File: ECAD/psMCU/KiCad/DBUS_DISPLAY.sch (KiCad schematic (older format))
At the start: 9 parts, among them U50 SN74LVC1G04DCK, U51 SN74HC245PW

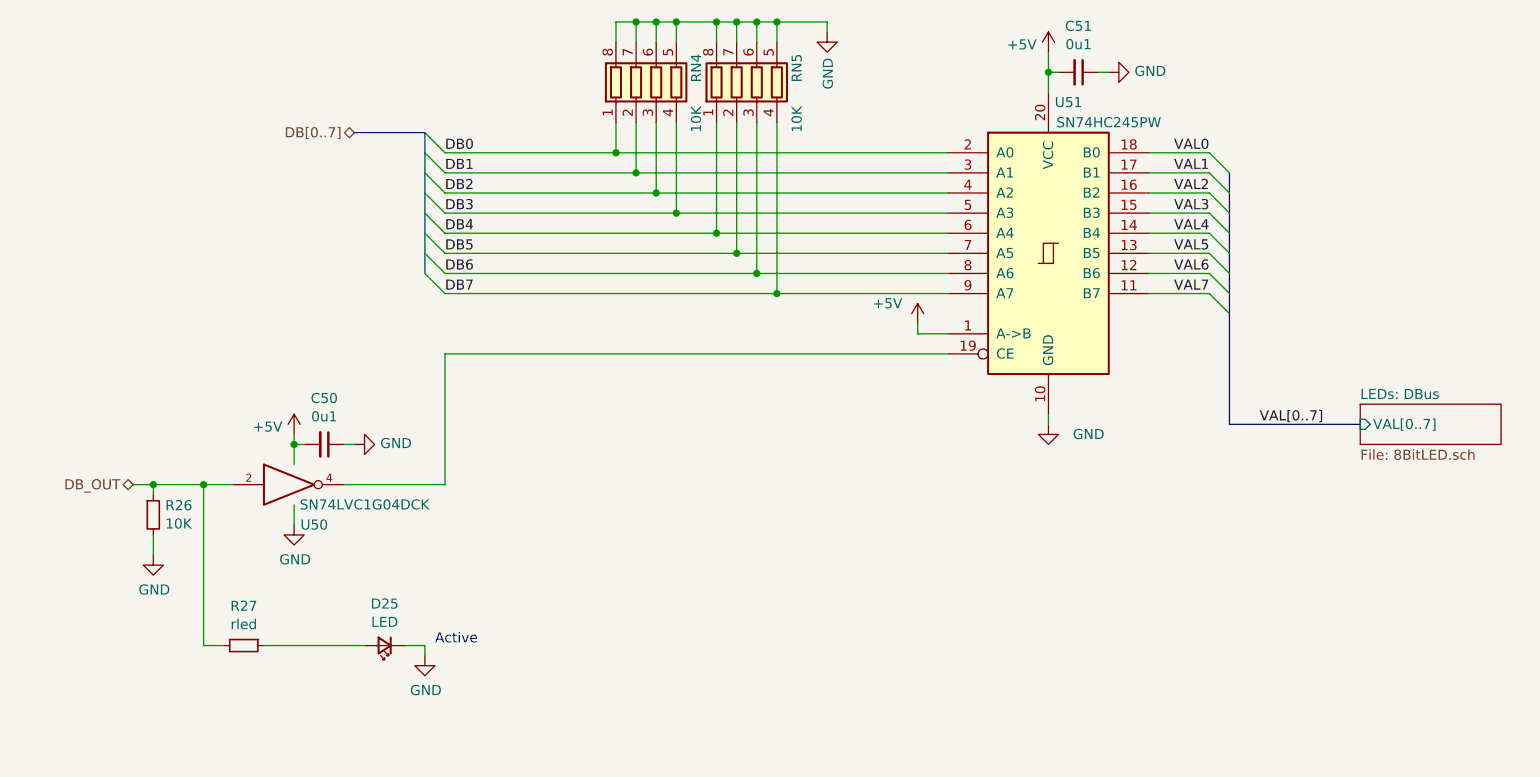
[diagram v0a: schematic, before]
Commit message: Sch: Reworked Peripheral Interface (Buffers)
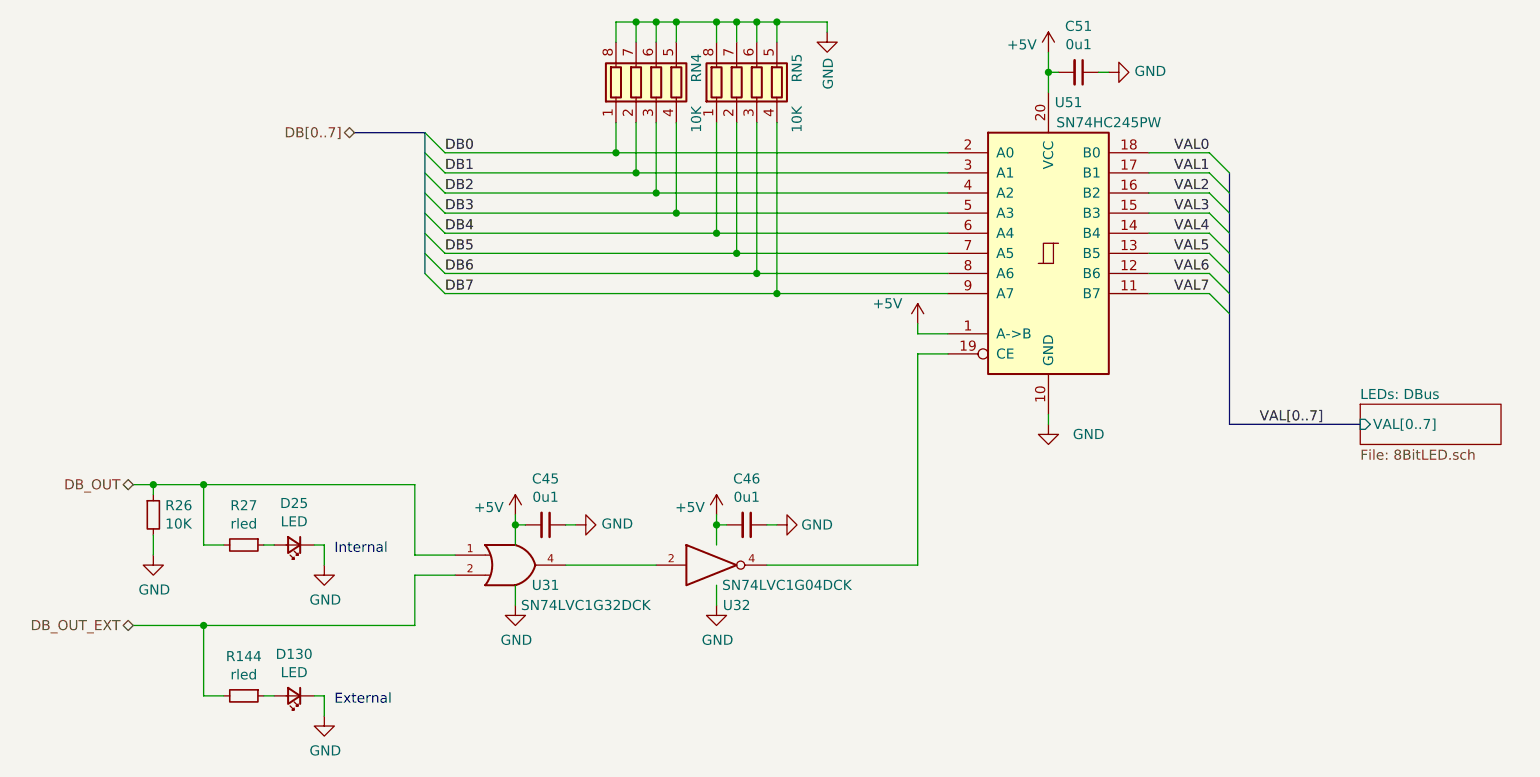
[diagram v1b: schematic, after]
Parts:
- removed C50: 0u1, NoRef_Footprints:C_0603_1608Metric_NoRef, symbol Device:C_Small
- removed U50: SN74LVC1G04DCK, Package_TO_SOT_SMD:SOT-353_SC-70-5, symbol 74xGxx:74LVC1G04
- added C45, C46: 0u1, NoRef_Footprints:C_0603_1608Metric_NoRef, symbol Device:C_Small
- added D130: LED, NoRef_Footprints:D_0603_1608Metric_NoRef, symbol Device:LED_Small
- added R144: rled, NoRef_Footprints:R_0603_1608Metric_NoRef, symbol Device:R_Small
- added U31: SN74LVC1G32DCK, Package_TO_SOT_SMD:SOT-353_SC-70-5, symbol 74xGxx:74LVC1G32
- added U32: SN74LVC1G04DCK, Package_TO_SOT_SMD:SOT-353_SC-70-5, symbol 74xGxx:74LVC1G04
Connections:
- net +5V: now also C45.2, C46.2, U31.5 (VCC), U32.5 (VCC)
- net DB_OUT: now also U31.1
- net GND: now also C45.1, C46.1, D130.1 (K), U31.3 (GND), U32.3 (GND)
- net at U51.19 (CE): now also U32.4
- new net: D130.2 (A), R144.1
- new net: U31.4, U32.2
- new net DB_OUT_EXT: R144.2, U31.2
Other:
- note added: "External"
- note added: "Internal"
- note removed: "Active"
- moved on the sheet: D25, R27
